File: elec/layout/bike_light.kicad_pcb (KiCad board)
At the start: 2 copper layers, 14 parts

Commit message: lay things out
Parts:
- added D1: , bike_light_lib:LED-SMD_3P-L7.0-W3.5_XL-C3570P5S10-62C3C2, F.Cu at (111.5, 106.0)
- added D3: , bike_light_lib:LED-SMD_3P-L7.0-W3.5_XL-C3570P5S10-62C3C2, F.Cu at (128.5, 106.1)
- added D4: , Diode_SMD:D_SOD-123, F.Cu at (113.2, 115.2)
- added D5: , Diode_SMD:D_SOD-123, F.Cu at (112.5, 125.8)
- added L1: 2uH, bike_light_lib:IND-SMD_L2.5-W2.0_SLW252012P, F.Cu at (118.0, 115.2)
- added U2: , bike_light_lib:SOT-223_L6.5-W3.5-P2.30-LS7.0-BR, F.Cu at (130.5, 116.0)
- added U3: , bike_light_lib:SOT-23-3_L2.9-W1.3-P1.90-LS2.4-BR, F.Cu at (105.0, 122.0)
- D2: footprint Diode_SMD:D_SOD-123 -> bike_light_lib:LED-SMD_3P-L7.0-W3.5_XL-C3570P5S10-62C3C2
- moved J2 88.5 mm to (111.2, 136.0), turned to 90 degrees
- moved R3 81.3 mm to (107.5, 126.0), turned to -90 degrees
- moved C4 80.6 mm to (103.5, 126.0), turned to 90 degrees
- moved R2 79.7 mm to (108.0, 114.3), turned to 90 degrees
- moved C2 75.8 mm to (108.0, 118.3), turned to -90 degrees
- moved U1 74.7 mm to (118.0, 120.5)
- moved J1 72.9 mm to (126.0, 134.9)
- moved R1 71.3 mm to (112.2, 120.4), turned to 90 degrees
- moved R4 71.2 mm to (118.0, 129.5)
- moved C3 66.5 mm to (118.0, 125.1)
- moved D2 66.3 mm to (120.1, 106.0), turned to 90 degrees
- moved R5 63.6 mm to (124.2, 123.0), turned to -90 degrees
- moved C1 59.8 mm to (126.5, 126.8)
- moved R6 59.2 mm to (128.5, 123.0), turned to 90 degrees
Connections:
- net 13 renamed 17
- net 27 renamed 31
- net 34 renamed 38
- net 35 renamed 39
- net 36 renamed 40
- C1 pad 1: (no net) -> 1
- C1 pad 2: (no net) -> 2
- C2 pad 1: 7 -> 11
- C2 pad 2: (no net) -> 2
- C3 pad 1: 11 -> 15
- C3 pad 2: (no net) -> 2
- C4 pad 2: (no net) -> 2
- D2 pad 1: 15 -> 7
- D2 pad 2: 7 -> 4
- J1 pad 1: (no net) -> 2
- J1 pad 2: (no net) -> 2
- J1 pad 3: (no net) -> 2
- J1 pad 4: (no net) -> 2
- J1 pad A1: (no net) -> 2
- J1 pad A12: (no net) -> 2
- J1 pad A4: 41 -> 1
- J1 pad A8: 37 -> 41
- J1 pad A9: 41 -> 1
- J1 pad B1: (no net) -> 2
- J1 pad B12: (no net) -> 2
- J1 pad B4: 41 -> 1
- J1 pad B8: 37 -> 41
- J1 pad B9: 41 -> 1
- J2 pad 1: 8 -> 2
- J2 pad 2: (no net) -> 12
- R1 pad 1: 10 -> 14
- R1 pad 2: (no net) -> 2
- R2 pad 1: 7 -> 11
- R3 pad 1: 25 -> 29
- R4 pad 1: 8 -> 12
- R4 pad 2: (no net) -> 2
- R5 pad 1: 7 -> 11
- R6 pad 2: (no net) -> 2
- U1 pad 10: 14 -> 18
- U1 pad 11: (no net) -> 1
- U1 pad 12: (no net) -> 1
- U1 pad 13: 7 -> 11
- U1 pad 15: (no net) -> 1
- U1 pad 16: (no net) -> 1
- U1 pad 17: (no net) -> 2
- U1 pad 18: 15 -> 19
- U1 pad 3: (no net) -> 1
- U1 pad 4: 10 -> 14
- U1 pad 5: (no net) -> 1
- U1 pad 6: 11 -> 15
- U1 pad 7: 12 -> 16
- U1 pad 9: 14 -> 18
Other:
- board outline added: 40 x 40 mm

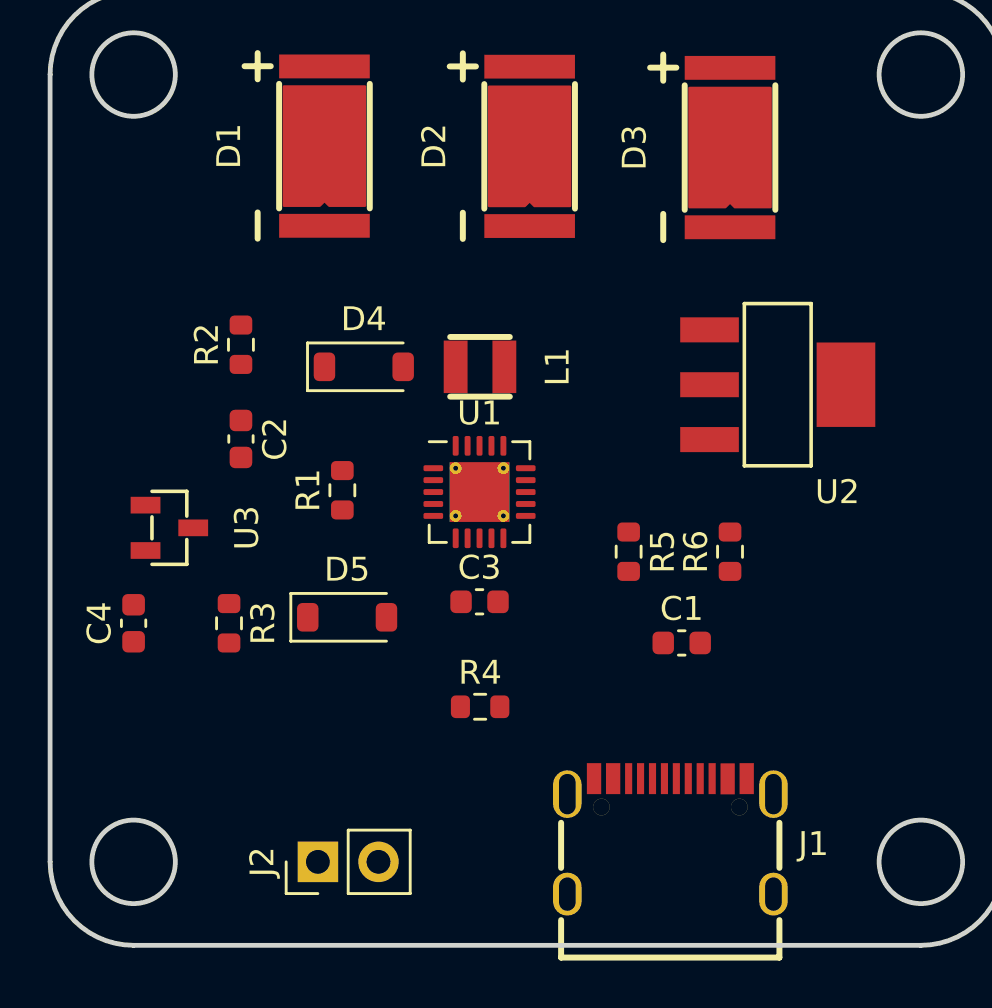
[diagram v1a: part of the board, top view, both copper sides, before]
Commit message: move nmos around
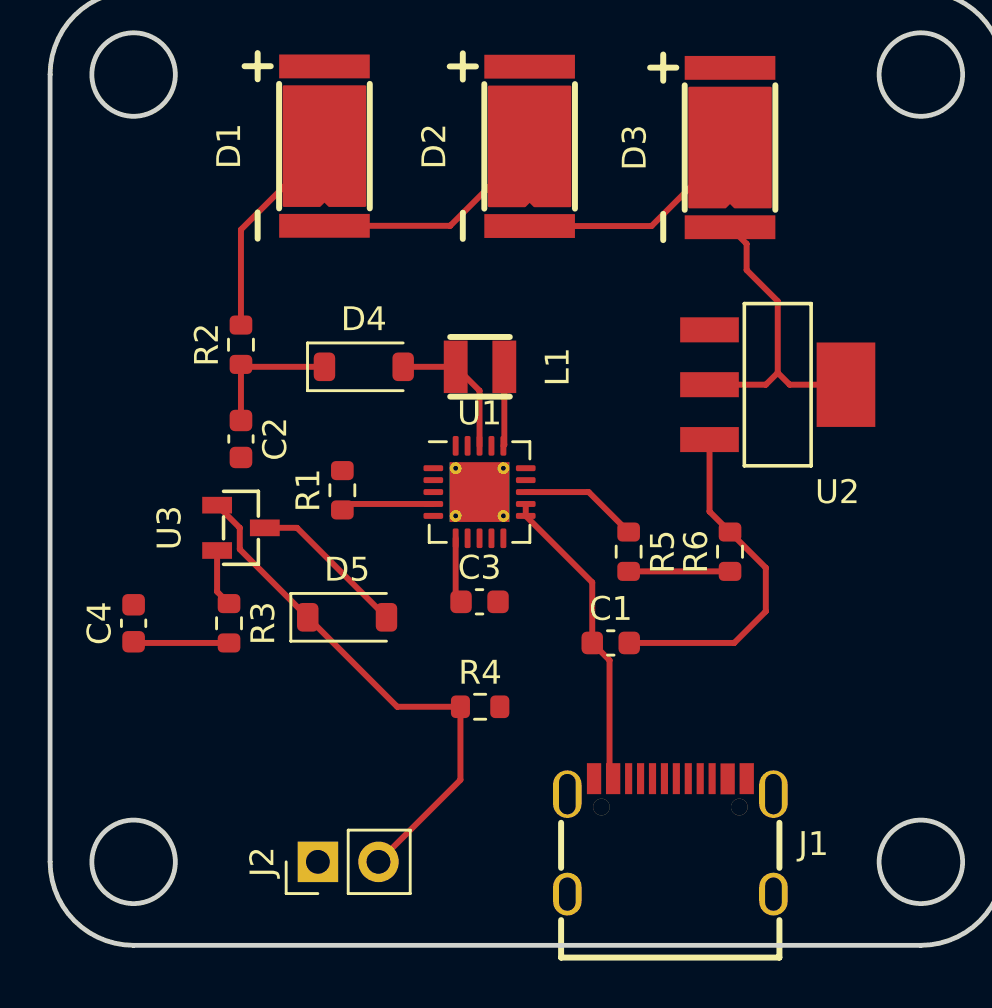
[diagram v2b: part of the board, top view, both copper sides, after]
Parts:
- moved U3 3.00 mm to (108.0, 122.0)
- moved C1 2.97 mm to (123.5, 126.8)
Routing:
- net 12: track 0.00 -> 22.2 mm
- net 1: track 0.00 -> 16.3 mm
- net 2: track 0.00 -> 14.5 mm
- net 9: track 0.00 -> 13.1 mm
- net 11: track 0.00 -> 10.9 mm
- net 4: track 0.00 -> 9.98 mm
- net 7: track 0.00 -> 9.76 mm
- net 5: track 0.00 -> 8.95 mm
- net 16: track 0.00 -> 6.65 mm
- net 19: track 0.00 -> 5.93 mm
- net 17: track 0.00 -> 4.25 mm
- net 31: track 0.00 -> 4.02 mm
- net 14: track 0.00 -> 3.92 mm
- net 15: track 0.00 -> 2.76 mm
- net 29: track 0.00 -> 2.43 mm
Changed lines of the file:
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@@
   )
   (footprint "bike_light_lib:SOT-23-3_L2.9-W1.3-P1.90-LS2.4-BR" (layer "F.Cu")
-    (at 105 122 180)
-    (attr smd)
-    (fp_text reference "U3" (at -3.25 0 90) (layer "F.SilkS")
+    (at 108 122 180)
+    (attr smd)
+    (fp_text reference "U3" (at 3 0 90) (layer "F.SilkS")
         (effects (font (size 1 1) (thickness 0.15)))
     )
@@
   )
   (footprint "Capacitor_SMD:C_0603_1608Metric" (layer "F.Cu")
-    (at 126.475 126.825)
+    (at 123.5 126.825)
     (descr "Capacitor SMD 0603 (1608 Metric), square (rectangular) end terminal, IPC_7351 nominal, (Body size source: IPC-SM-782 page 76, https://www.pcb-3d.com/wordpress/wp-content/uploads/ipc-sm-782a_amendment_1_and_2.pdf), generated with kicad-footprint-generator")
     (tags "capacitor")
@@
   (gr_line (start 103.5 99.5) (end 136.5 99.5)
     (stroke (width 0.2) (type solid)) (layer "Edge.Cuts"))
+  (segment (start 110.8 125.75) (end 107.95 122.9) (width 0.25) (layer "F.Cu") (net 1))
+  (segment (start 117.2 132.565) (end 117.2 129.5) (width 0.25) (layer "F.Cu") (net 1))
+  (segment (start 117.2 129.5) (end 114.55 129.5) (width 0.25) (layer "F.Cu") (net 1))
+  (segment (start 113.765 136) (end 117.2 132.565) (width 0.25) (layer "F.Cu") (net 1))
+  (segment (start 107.95 122) (end 107 121.05) (width 0.25) (layer "F.Cu") (net 1))
+  (segment (start 114.55 129.5) (end 110.8 125.75) (width 0.25) (layer "F.Cu") (net 1))
+  (segment (start 107.95 122.9) (end 107.95 122) (width 0.25) (layer "F.Cu") (net 1))
+  (segment (start 127.64 121.315) (end 127.64 118.3) (width 0.25) (layer "F.Cu") (net 2))
+  (segment (start 124.275 126.825) (end 128.675 126.825) (width 0.25) (layer "F.Cu") (net 2))
+  (segment (start 130 123.675) (end 128.5 122.175) (width 0.25) (layer "F.Cu") (net 2))
+  (segment (start 128.675 126.825) (end 130 125.5) (width 0.25) (layer "F.Cu") (net 2))
+  (segment (start 130 125.5) (end 130 123.675) (width 0.25) (layer "F.Cu") (net 2))
+  (segment (start 128.5 122.175) (end 127.64 121.315) (width 0.25) (layer "F.Cu") (net 2))
+  (segment (start 108 109.5) (end 111.5 106) (width 0.25) (layer "F.Cu") (net 3))
+  (segment (start 108 113.5) (end 108 109.5) (width 0.25) (layer "F.Cu") (net 3))
+  (segment (start 119 118.5625) (end 119.04 118.5225) (width 0.25) (layer "F.Cu") (net 4))
+  (segment (start 123.45 127.55) (end 122.725 126.825) (width 0.25) (layer "F.Cu") (net 4))
+  (segment (start 122.725 124.2875) (end 119.9375 121.5) (width 0.25) (layer "F.Cu") (net 4))
+  (segment (start 119.04 118.5225) (end 119.04 115.25) (width 0.25) (layer "F.Cu") (net 4))
+  (segment (start 119.9375 121.5) (end 119.9375 121) (width 0.25) (layer "F.Cu") (net 4))
+  (segment (start 123.45 132.5125) (end 123.45 127.55) (width 0.25) (layer "F.Cu") (net 4))
+  (segment (start 122.725 126.825) (end 122.725 124.2875) (width 0.25) (layer "F.Cu") (net 4))
+  (segment (start 117.225 125.1) (end 117 124.875) (width 0.25) (layer "F.Cu") (net 6))
+  (segment (start 117 124.875) (end 117 122.4375) (width 0.25) (layer "F.Cu") (net 6))
+  (segment (start 120.1 109.35) (end 125.21 109.35) (width 0.25) (layer "F.Cu") (net 7))
+  (segment (start 125.21 109.35) (end 128.5 106.06) (width 0.25) (layer "F.Cu") (net 7))
+  (segment (start 112.5 121) (end 112.25 121.25) (width 0.25) (layer "F.Cu") (net 9))
+  (segment (start 116.0625 121) (end 112.5 121) (width 0.25) (layer "F.Cu") (net 9))
+  (segment (start 107 124.675) (end 107.5 125.175) (width 0.25) (layer "F.Cu") (net 11))
+  (segment (start 107 122.95) (end 107 124.675) (width 0.25) (layer "F.Cu") (net 11))
+  (segment (start 110.35 122) (end 114.1 125.75) (width 0.25) (layer "F.Cu") (net 12))
+  (segment (start 109 122) (end 110.35 122) (width 0.25) (layer "F.Cu") (net 12))
+  (segment (start 129.195 111.195) (end 130.5 112.5) (width 0.25) (layer "F.Cu") (net 13))
+  (segment (start 130.5 115.5) (end 130 116) (width 0.25) (layer "F.Cu") (net 13))
+  (segment (start 129.195 110.095) (end 129.195 111.195) (width 0.25) (layer "F.Cu") (net 13))
+  (segment (start 130 116) (end 127.64 116) (width 0.25) (layer "F.Cu") (net 13))
+  (segment (start 130.5 112.5) (end 130.5 115.5) (width 0.25) (layer "F.Cu") (net 13))
+  (segment (start 133.36 116) (end 131 116) (width 0.25) (layer "F.Cu") (net 13))
+  (segment (start 128.5 109.4) (end 129.195 110.095) (width 0.25) (layer "F.Cu") (net 13))
+  (segment (start 131 116) (end 130.5 115.5) (width 0.25) (layer "F.Cu") (net 13))
+  (segment (start 116.77 109.34) (end 120.1 106.01) (width 0.25) (layer "F.Cu") (net 14))
+  (segment (start 111.5 109.34) (end 116.77 109.34) (width 0.25) (layer "F.Cu") (net 14))
+  (segment (start 108.1 115.25) (end 108 115.15) (width 0.25) (layer "F.Cu") (net 15))
+  (segment (start 108 115.15) (end 108 117.5) (width 0.25) (layer "F.Cu") (net 15))
+  (segment (start 111.5 115.25) (end 108.1 115.25) (width 0.25) (layer "F.Cu") (net 15))
+  (segment (start 122.575 120.5) (end 124.25 122.175) (width 0.25) (layer "F.Cu") (net 15))
+  (segment (start 119.9375 120.5) (end 122.575 120.5) (width 0.25) (layer "F.Cu") (net 15))
+  (segment (start 118 118.5625) (end 118 116.25) (width 0.25) (layer "F.Cu") (net 17))
+  (segment (start 118 116.25) (end 117 115.25) (width 0.25) (layer "F.Cu") (net 17))
+  (segment (start 117 115.25) (end 114.8 115.25) (width 0.25) (layer "F.Cu") (net 17))
+  (segment (start 107.5 126.825) (end 103.55 126.825) (width 0.25) (layer "F.Cu") (net 18))
+  (segment (start 103.55 126.825) (end 103.5 126.775) (width 0.25) (layer "F.Cu") (net 18))
+  (segment (start 124.25 123.825) (end 128.5 123.825) (width 0.25) (layer "F.Cu") (net 19))
   (group "" (id ba4d4596-1074-4429-bbeb-256b845808bd)
     (members
